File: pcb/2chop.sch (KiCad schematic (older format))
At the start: 7 parts, among them U1 TL082

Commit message: Schematic almost done
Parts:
- added C? (x2): NI, symbol C
- added C? (x2): 39pF, symbol C
- added C? (x2): 100nF, symbol C
- added C? (x2): 2200pF, symbol C
- added K? (x2): CONN_3, symbol CONN_3
- added P?: CONN_5X2, symbol CONN_5X2
- added R? (x2): 1K, symbol R
- added R? (x2): NI, symbol R
- added R? (x2): 0, symbol R
- added R? (x2): 10, symbol R
- R? (x2): value R -> 1K
- R? (x2): value R -> NI
- R? (x2): value R -> 0
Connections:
- net at U1.1: now also K?.1 (P1), R?.2
- net at U1.2 (-): now also C?.1, R?.1, R?.2, R?.2
- net at U1.3 (+): now also R?.2
- net -14: now reaches U1.4 (V-)
- net -14: now also U1.4 (V-), C?.2, P?.5
- net +14: now reaches U1.8 (V+)
- net +14: now also U1.8 (V+), C?.2, P?.7
- net at R?.1, R?.2, R?.2: now also U1.6 (-), C?.1; no longer U1.5 (+)
- net at R?.2: now also U1.5 (+); no longer U1.6 (-)
- net at R?.2, U1.7: now also K?.1 (P1)
- net AGND: now reaches R?.1
- net AGND: now also R?.1, C?.1, C?.1, C?.1, C?.1, C?.2, C?.2, P?.10, R?.1, R?.1
- net at R?.1, R?.2: now also K?.3 (P3), P?.1
- net at R?.1, R?.1, R?.2: now also C?.1
- new net: K?.3 (P3), P?.3, R?.1, R?.2
- new net: C?.1, R?.1, R?.1, R?.2
- new net: K?.2 (PM), R?.1 (x2)
- new net 5v: P?.9
- new net OUT1: C?.2, R?.2
- new net OUT2: C?.2, R?.2
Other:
- moved on the sheet: U1A

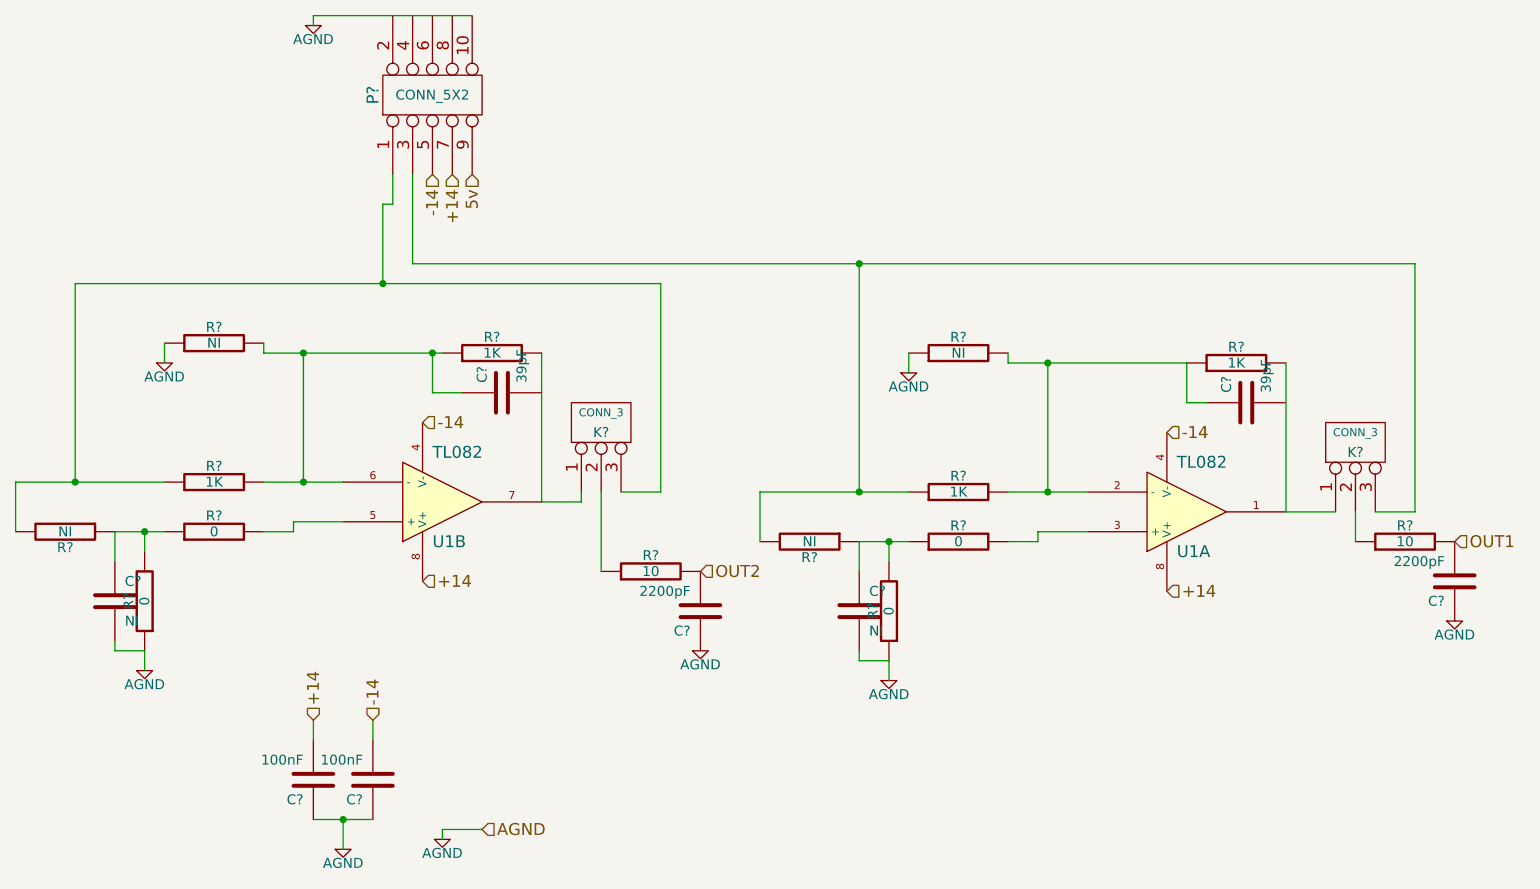
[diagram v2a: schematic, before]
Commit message: fixed all pcb components
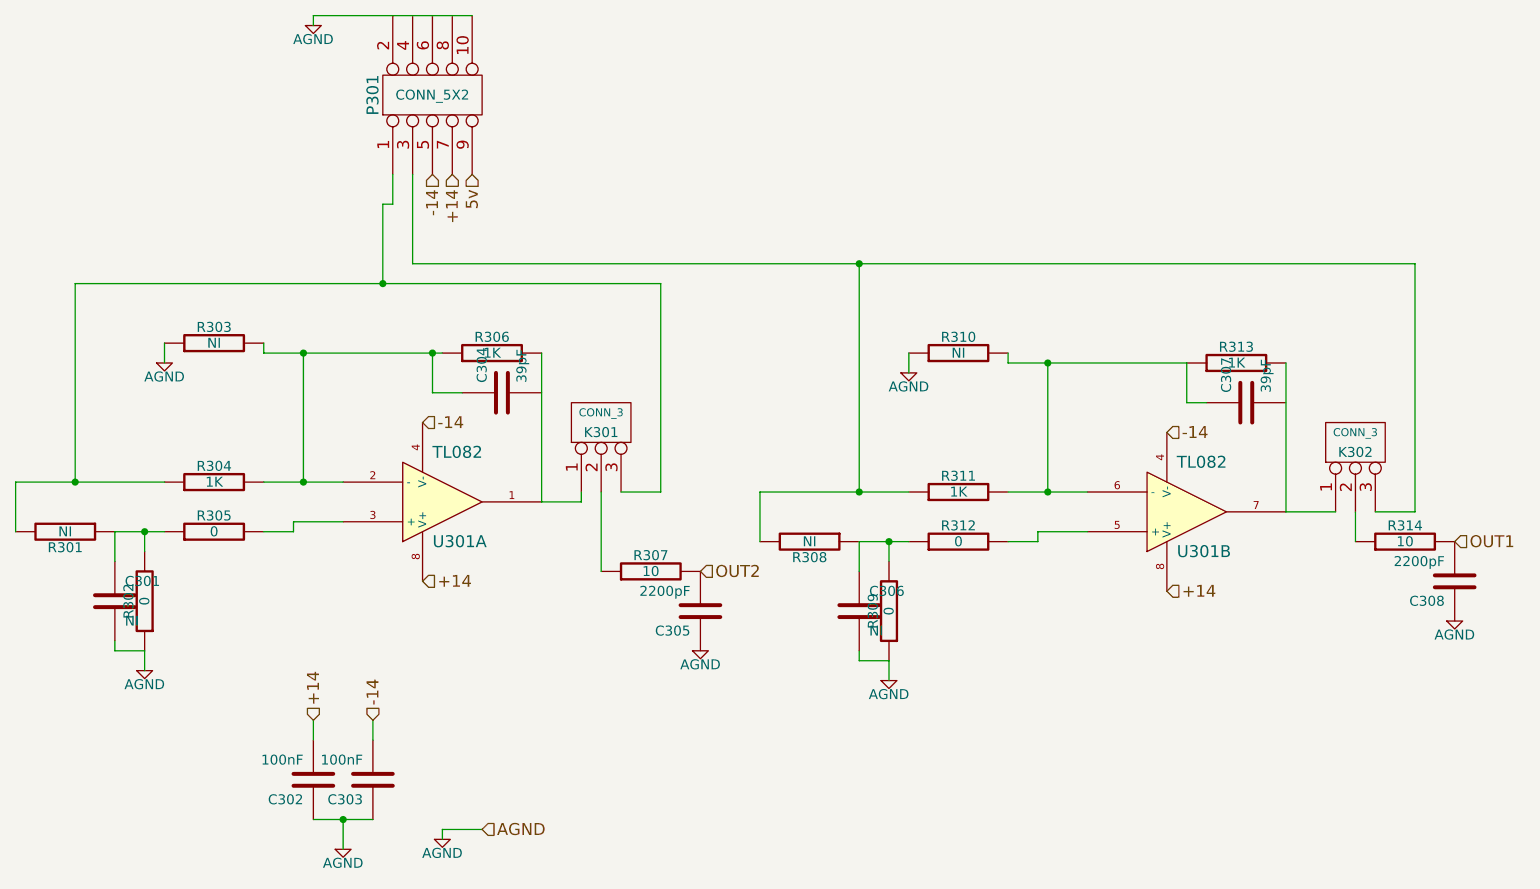
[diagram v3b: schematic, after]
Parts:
- gave numbers to parts that had none: 25
- renumbered U1 to U301
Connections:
- net at K302.1 (P1), R313.2: now also U301.7; no longer U301.1
- net at C307.1, R310.2, R311.2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: now also U301.6 (-); no longer U301.2 (-)
- net at R312.2: now also U301.5 (+); no longer U301.3 (+)
- net at R305.2: now also U301.3 (+); no longer U301.5 (+)
- net at C304.1, R303.2, R304.2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: now also U301.2 (-); no longer U301.6 (-)
- net at K301.1 (P1), R306.2: now also U301.1; no longer U301.7
